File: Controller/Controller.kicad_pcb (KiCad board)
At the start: 2 copper layers, 213 x 25 mm, 91 parts, among them J1 CON_TLC, J2 CON_15V, J3 CON_ICSP, J4 DC out, J5 CON_5V, J6 CON_5V_AUX, J7 CON_USB_A, Q1 SI4435FDY, Q2 SI4435FDY, Q3 SQ2309ES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

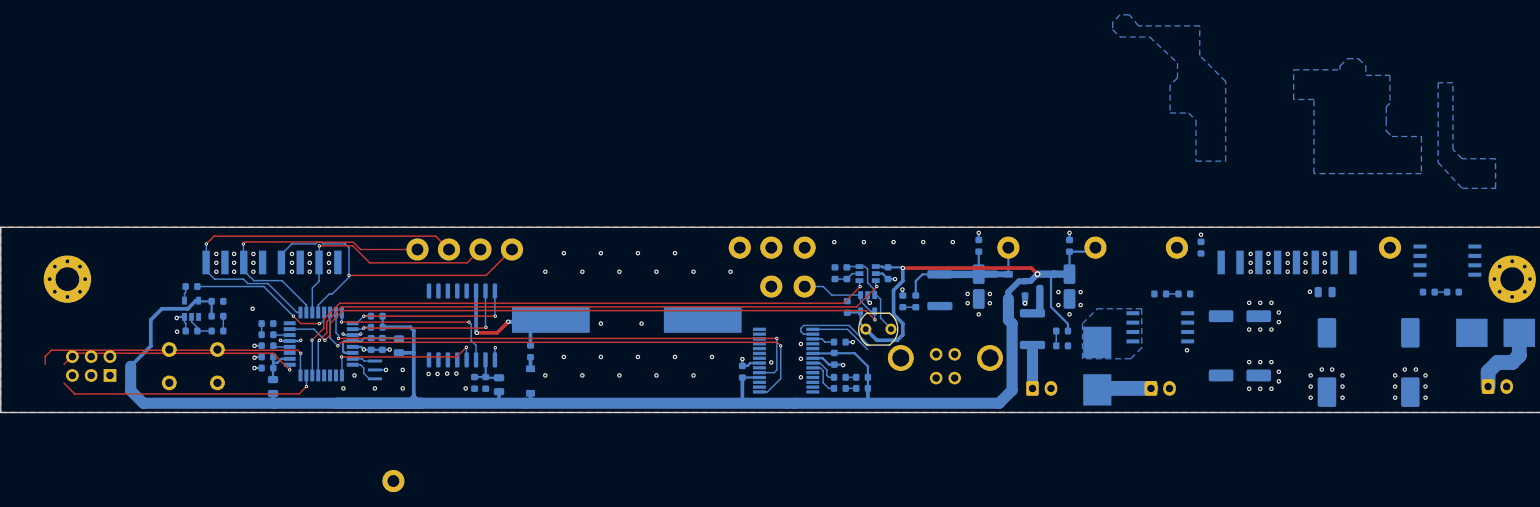
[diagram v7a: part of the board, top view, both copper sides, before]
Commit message: Modified controller layout. Fixed distance to board edge.
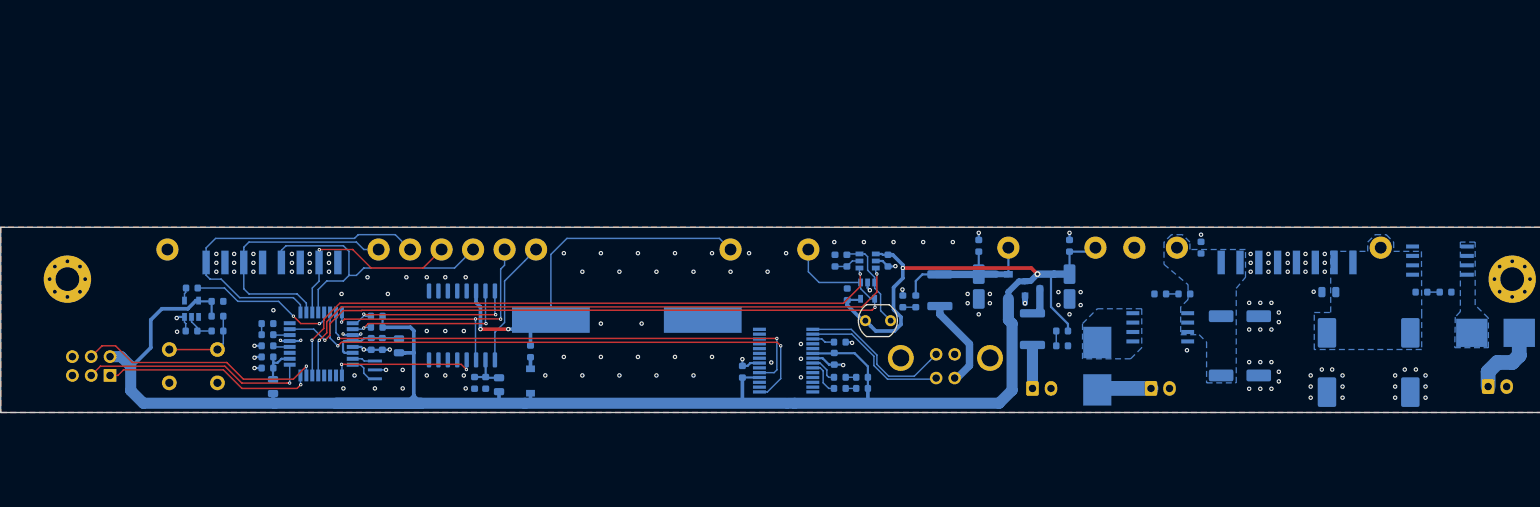
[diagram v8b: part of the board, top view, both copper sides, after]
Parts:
- added G***: LOGO, ak:lemonhead, F.Cu at (64.8, 102.8)
- added G***: LOGO, ak:logo-mask, F.Cu at (239.0, 104.0)
- added G***: LOGO, ak:LN-10x5mm, B.Cu at (153.0, 103.0)
- moved TP4 104.8 mm to (199.5, 95.8)
- moved TP2 81.7 mm to (69.0, 96.0)
- moved TP1 31.8 mm to (114.5, 96.0)
- moved TP3 31.8 mm to (118.8, 96.0)
- moved TP12 10.0 mm to (145.0, 96.0)
- moved TP10 5.25 mm to (97.5, 96.0)
- moved TP11 5.25 mm to (101.8, 96.0)
- moved TP7 5.25 mm to (106.0, 96.0)
- moved TP9 5.25 mm to (110.2, 96.0)
- moved TP5 5.02 mm to (155.5, 96.0)
- moved C22 1.70 mm to (160.8, 102.0)
- moved C23 1.70 mm to (160.7, 97.5)
- moved C25 1.70 mm to (166.2, 97.5)
- moved R15 1.70 mm to (159.1, 97.5)
- moved U5 1.70 mm to (163.5, 101.5)
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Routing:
- net +BATT: track 15.8 -> 50.0 mm
- net /RTC_32K: track 1.67 -> 17.2 mm, vias 1 -> 0
- net /RTC_1PPS: track 24.2 -> 38.3 mm, vias 2 -> 3
- net /USBD+: track 8.53 -> 21.2 mm
- net Net-(F4-Pad2): track 0.00 -> 12.4 mm
- net /MISO: track 39.1 -> 28.6 mm
- net Net-(R11-Pad1): track 2.00 -> 11.3 mm
- net /USBD-: track 12.7 -> 20.0 mm
- net /TLC_SDA: track 34.3 -> 28.9 mm
- net /TLC_SCL: track 45.4 -> 40.8 mm, vias 1 -> 0
- net /TLC_BLANK: track 52.6 -> 48.2 mm, vias 1 -> 0
- net +5V: track 279.3 -> 283.5 mm
- net /TLC_LAT: track 39.0 -> 35.0 mm, vias 1 -> 0
- net /LDR: track 95.2 -> 97.5 mm
- net /POT_U~D~: track 84.8 -> 86.9 mm
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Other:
- board text added: "7 Segment Clock Controller"
- board text added: "GND"
- board text added: "REV. A 10/2019"
